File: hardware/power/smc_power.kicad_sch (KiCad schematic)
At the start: 64 parts, among them IC1 LM393DR2GH, J1 Screw_Terminal_Input, J2 Screw_Terminal_Output, Q1 P40B10SL, U1 TPS54360DDA, U2 AP2112K-3.3, U3 TPS54360DDA, U4 TL431D, U5 MCP1416, U7 L78L12_SOT89

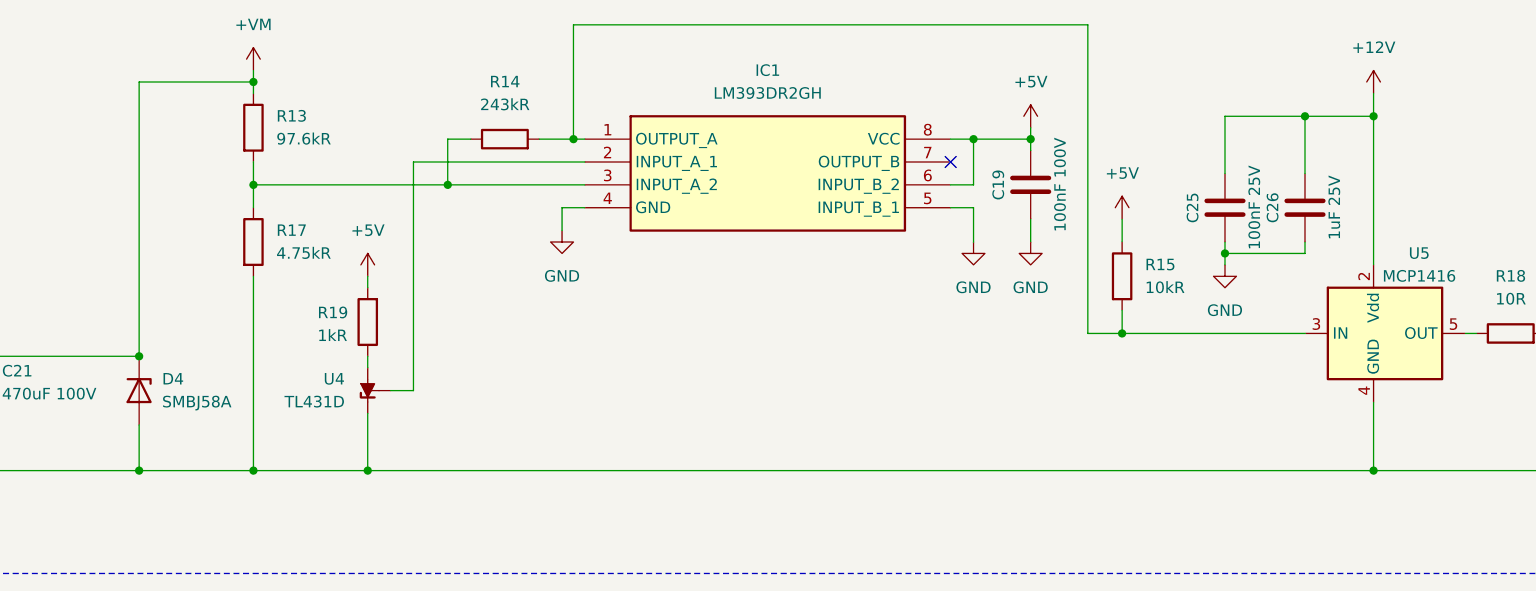
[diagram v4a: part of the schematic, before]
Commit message: hw(power): SMBJ51A TVS, fix TL431B (U4) orientation + REF-K, SOT-23 footprint, refs #35 #36 #37
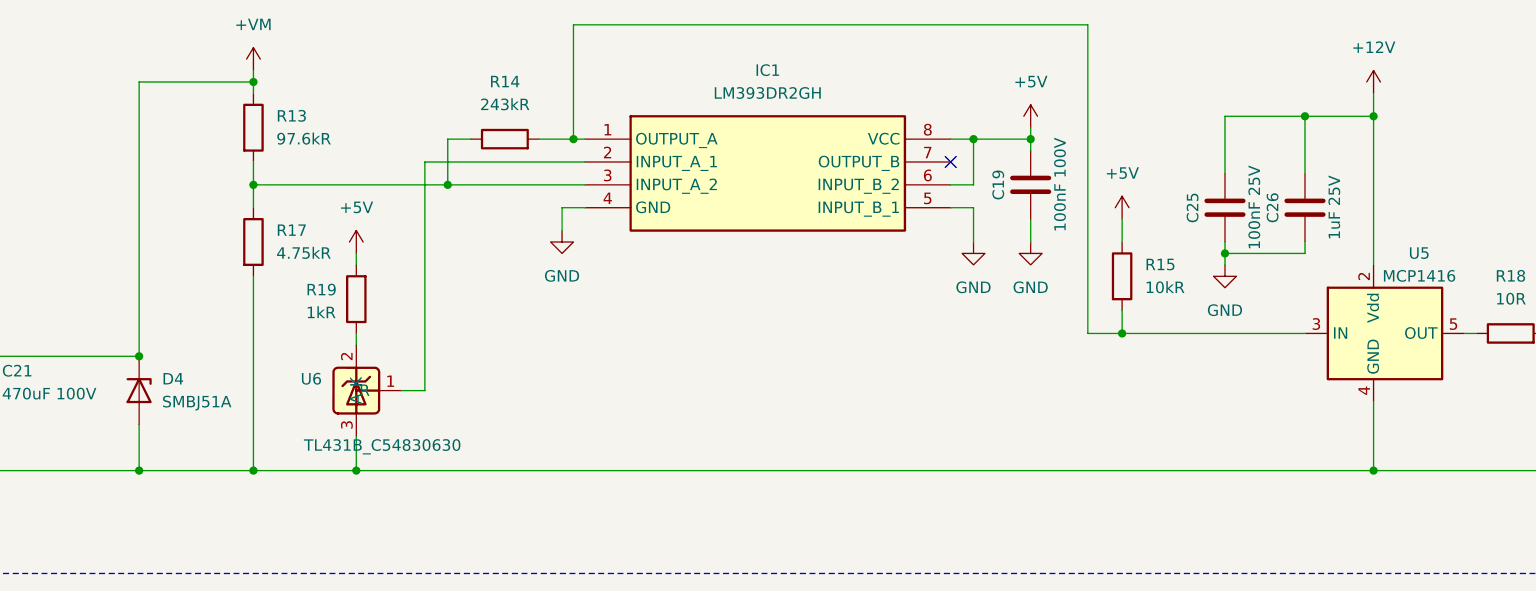
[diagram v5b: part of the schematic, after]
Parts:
- removed U4: TL431D, Package_SO:SOIC-8_3.9x4.9mm_P1.27mm, symbol Reference_Voltage:TL431D
- added U6: TL431B_C54830630, Package_TO_SOT_SMD:SOT-23-3, symbol JLCImport:TL431B_C54830630
- D4: value SMBJ58A -> SMBJ51A
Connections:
- net GND: now also U6.3 (A)
- net at R19.1: now also U6.2 (K)
- net at IC1.2 (INPUT_A_1): now also U6.1 (R)
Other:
- moved on the sheet: R19
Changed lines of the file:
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@@
 	)
 	(junction
-		(at 87.63 267.97)
-		(diameter 0)
-		(color 0 0 0 0)
-	)
-	(junction
 		(at 63.5 116.84)
 		(diameter 0)
@@
 	)
 	(junction
+		(at 86.36 267.97)
+		(diameter 0)
+		(color 0 0 0 0)
+	)
+	(junction
 		(at 62.23 167.64)
 		(diameter 0)
@@
 	(wire
 		(pts
+			(xy 86.36 264.16) (xy 86.36 267.97)
+		)
+		(stroke
+			(width 0)
+			(type default)
+		)
+	)
+	(wire
+		(pts
 			(xy 148.59 184.15) (xy 148.59 175.26)
 		)
@@
 	(wire
 		(pts
-			(xy 87.63 255.27) (xy 87.63 256.54)
+			(xy 86.36 252.73) (xy 86.36 254)
 		)
 		(stroke
@@
 	(wire
 		(pts
-			(xy 199.39 267.97) (xy 87.63 267.97)
+			(xy 74.93 267.97) (xy 86.36 267.97)
 		)
 		(stroke
@@
 	(wire
 		(pts
-			(xy 90.17 259.08) (xy 92.71 259.08)
-		)
-		(stroke
-			(width 0)
-			(type default)
-		)
-	)
-	(wire
-		(pts
 			(xy 114.3 121.92) (xy 114.3 137.16)
 		)
@@
 	(wire
 		(pts
-			(xy 87.63 246.38) (xy 87.63 247.65)
+			(xy 86.36 243.84) (xy 86.36 245.11)
 		)
 		(stroke
@@
 	(wire
 		(pts
-			(xy 92.71 233.68) (xy 111.76 233.68)
+			(xy 93.98 233.68) (xy 111.76 233.68)
 		)
 		(stroke
@@
 	(wire
 		(pts
+			(xy 86.36 267.97) (xy 199.39 267.97)
+		)
+		(stroke
+			(width 0)
+			(type default)
+		)
+	)
+	(wire
+		(pts
 			(xy 259.08 167.64) (xy 267.97 167.64)
 		)
@@
 	(wire
 		(pts
-			(xy 92.71 259.08) (xy 92.71 233.68)
+			(xy 93.98 259.08) (xy 93.98 233.68)
 		)
 		(stroke
@@
 	(wire
 		(pts
+			(xy 91.44 259.08) (xy 93.98 259.08)
+		)
+		(stroke
+			(width 0)
+			(type default)
+		)
+	)
+	(wire
+		(pts
 			(xy 181.61 185.42) (xy 181.61 187.96)
 		)
@@
 	(wire
 		(pts
-			(xy 74.93 267.97) (xy 87.63 267.97)
-		)
-		(stroke
-			(width 0)
-			(type default)
-		)
-	)
-	(wire
-		(pts
 			(xy 181.61 172.72) (xy 176.53 172.72)
 		)
@@
 	(wire
 		(pts
-			(xy 87.63 261.62) (xy 87.63 267.97)
-		)
-		(stroke
-			(width 0)
-			(type default)
-		)
-	)
-	(wire
-		(pts
 			(xy 134.62 198.12) (xy 134.62 200.66)
 		)
@@
 	(symbol
 		(lib_id "Device:R")
-		(at 87.63 251.46 180)
+		(at 86.36 248.92 180)
 		(unit 1)
 		(body_style 1)
@@
 		(dnp no)
 		(property "Reference" "R19"
-			(at 82.042 250.444 0)
+			(at 80.772 247.904 0)
 			(show_name no)
 			(do_not_autoplace no)
@@
 		)
 		(property "Value" "1kR"
-			(at 82.042 252.984 0)
+			(at 80.772 250.444 0)
 			(show_name no)
 			(do_not_autoplace no)
@@
 		)
 		(property "Footprint" "Resistor_SMD:R_0805_2012Metric_Pad1.20x1.40mm_HandSolder"
-			(at 89.408 251.46 90)
+			(at 88.138 248.92 90)
 			(hide yes)
 			(show_name no)
@@
 		)
 		(property "Datasheet" ""
-			(at 87.63 251.46 0)
+			(at 86.36 248.92 0)
 			(hide yes)
 			(show_name no)
@@
 		)
 		(property "Description" "Resistor"
-			(at 87.63 251.46 0)
+			(at 86.36 248.92 0)
 			(hide yes)
 			(show_name no)
@@
 	(symbol
 		(lib_id "power:+5V")
-		(at 87.63 246.38 0)
+		(at 86.36 243.84 0)
 		(unit 1)
 		(body_style 1)
@@
 		(fields_autoplaced yes)
 		(property "Reference" "#PWR025"
-			(at 87.63 250.19 0)
+			(at 86.36 247.65 0)
 			(hide yes)
 			(show_name no)
@@
 		)
 		(property "Value" "+5V"
-			(at 87.63 241.3 0)
+			(at 86.36 238.76 0)
 			(show_name no)
 			(do_not_autoplace no)
@@
 		)
 		(property "Footprint" ""
-			(at 87.63 246.38 0)
+			(at 86.36 243.84 0)
 			(hide yes)
 			(show_name no)
@@
 		)
 		(property "Datasheet" ""
-			(at 87.63 246.38 0)
+			(at 86.36 243.84 0)
 			(hide yes)
 			(show_name no)
@@
 		)
 		(property "Description" "Power symbol creates a global label with name \"+5V\""
-			(at 87.63 246.38 0)
+			(at 86.36 243.84 0)
 			(hide yes)
 			(show_name no)
@@
 	)
 	(symbol
-		(lib_id "Reference_Voltage:TL431D")
-		(at 87.63 259.08 270)
-		(unit 1)
-		(body_style 1)
-		(exclude_from_sim no)
-		(in_bom yes)
-		(on_board yes)
-		(in_pos_files yes)
-		(dnp no)
-		(fields_autoplaced yes)
-		(property "Reference" "U4"
-			(at 85.09 257.8099 90)
-			(show_name no)
-			(do_not_autoplace no)
-			(effects
-				(font
-					(size 1.27 1.27)
-				)
-				(justify right)
-			)
-		)
-		(property "Value" "TL431D"
-			(at 85.09 260.3499 90)
-			(show_name no)
-			(do_not_autoplace no)
-			(effects
-				(font
-					(size 1.27 1.27)
-				)
-				(justify right)
-			)
-		)
-		(property "Footprint" "Package_SO:SOIC-8_3.9x4.9mm_P1.27mm"
-			(at 81.28 259.08 0)
-			(hide yes)
-			(show_name no)
-			(do_not_autoplace no)
-			(effects
-				(font
-					(size 1.27 1.27)
-					(italic yes)
-				)
-			)
-		)
-		(property "Datasheet" "http://www.ti.com/lit/ds/symlink/tl431.pdf"
-			(at 76.962 259.334 0)
-			(hide yes)
-			(show_name no)
-			(do_not_autoplace no)
-			(effects
-				(font
-					(size 1.27 1.27)
-					(italic yes)
-				)
-			)
-		)
-		(property "Description" "Shunt Regulator, SO-8"
-			(at 79.248 258.826 0)
-			(hide yes)
-			(show_name no)
-			(do_not_autoplace no)
-			(effects
-				(font
-					(size 1.27 1.27)
-				)
-			)
-		)
-		(pin "1"
-		)
-		(pin "8"
-		)
-		(pin "[2,3,6,7]"
-		)
-		(instances
-			(project "smc_power"
-				(path "/30583e29-7231-44d2-b6ef-f52f82bb6e27"
-					(reference "U4")
-					(unit 1)
-				)
-			)
-		)
-	)
-	(symbol
 		(lib_id "Regulator_Linear:AP2112K-3.3")
 		(at 284.48 114.3 0)
@@
 	)
 	(symbol
+		(lib_id "JLCImport:TL431B_C54830630")
+		(at 86.36 259.08 0)
+		(mirror y)
+		(unit 1)
+		(body_style 1)
+		(exclude_from_sim no)
+		(in_bom yes)
+		(on_board yes)
+		(in_pos_files yes)
+		(dnp no)
+		(property "Reference" "U6"
+			(at 82.55 257.8099 0)
+			(show_name no)
+			(do_not_autoplace no)
+			(effects
+				(font
+					(size 1.27 1.27)
+				)
+				(justify left)
+			)
+		)
+		(property "Value" "TL431B_C54830630"
+			(at 98.044 265.176 0)
+			(show_name no)
+			(do_not_autoplace no)
+			(effects
+				(font
+					(size 1.27 1.27)
+				)
+				(justify left)
+			)
+		)
+		(property "Footprint" "Package_TO_SOT_SMD:SOT-23-3"
+			(at 86.36 259.08 0)
+			(hide yes)
+			(show_name no)
+			(do_not_autoplace no)
+			(effects
+				(font
+					(size 1.27 1.27)
+				)
+			)
+		)
+		(property "Datasheet" "https://item.szlcsc.com/139341.html"
+			(at 86.36 259.08 0)
+			(hide yes)
+			(show_name no)
+			(do_not_autoplace no)
+			(effects
+				(font
+					(size 1.27 1.27)
+				)
+			)
+		)
+		(property "Description" "-20℃~+70℃@(Ta) 150mA 1uA 2.5V~36V 2.5V~36V 250uA Adjustable Parallel ±0.3% SOT-23 Voltage Reference ROHS"
+			(at 86.36 259.08 0)
+			(hide yes)
+			(show_name no)
+			(do_not_autoplace no)
+			(effects
+				(font
+					(size 1.27 1.27)
+				)
+			)
+		)
+		(property "LCSC" "C54830630"
+			(at 86.36 259.08 0)
+			(hide yes)
+			(show_name no)
+			(do_not_autoplace no)
+			(effects
+				(font
+					(size 1.27 1.27)
+				)
+			)
+		)
+		(property "Manufacturer" "hongjiacheng"
+			(at 86.36 259.08 0)
+			(hide yes)
+			(show_name no)
+			(do_not_autoplace no)
+			(effects
+				(font
+					(size 1.27 1.27)
+				)
+			)
+		)
+		(property "Manufacturer Part" "TL431B"
+			(at 86.36 259.08 0)
+			(hide yes)
+			(show_name no)
+			(do_not_autoplace no)
+			(effects
+				(font
+					(size 1.27 1.27)
+				)
+			)
+		)
+		(pin "3"
+		)
+		(pin "1"
+		)
+		(pin "2"
+		)
+		(instances
+			(project "smc_power"
+				(path "/30583e29-7231-44d2-b6ef-f52f82bb6e27"
+					(reference "U6")
+					(unit 1)
+				)
+			)
+		)
+	)
+	(symbol
 		(lib_id "Device:R")
 		(at 135.89 118.11 0)
@@
 			)
 		)
-		(property "Value" "SMBJ58A"
+		(property "Value" "SMBJ51A"
 			(at 64.77 260.3499 90)
 			(show_name no)

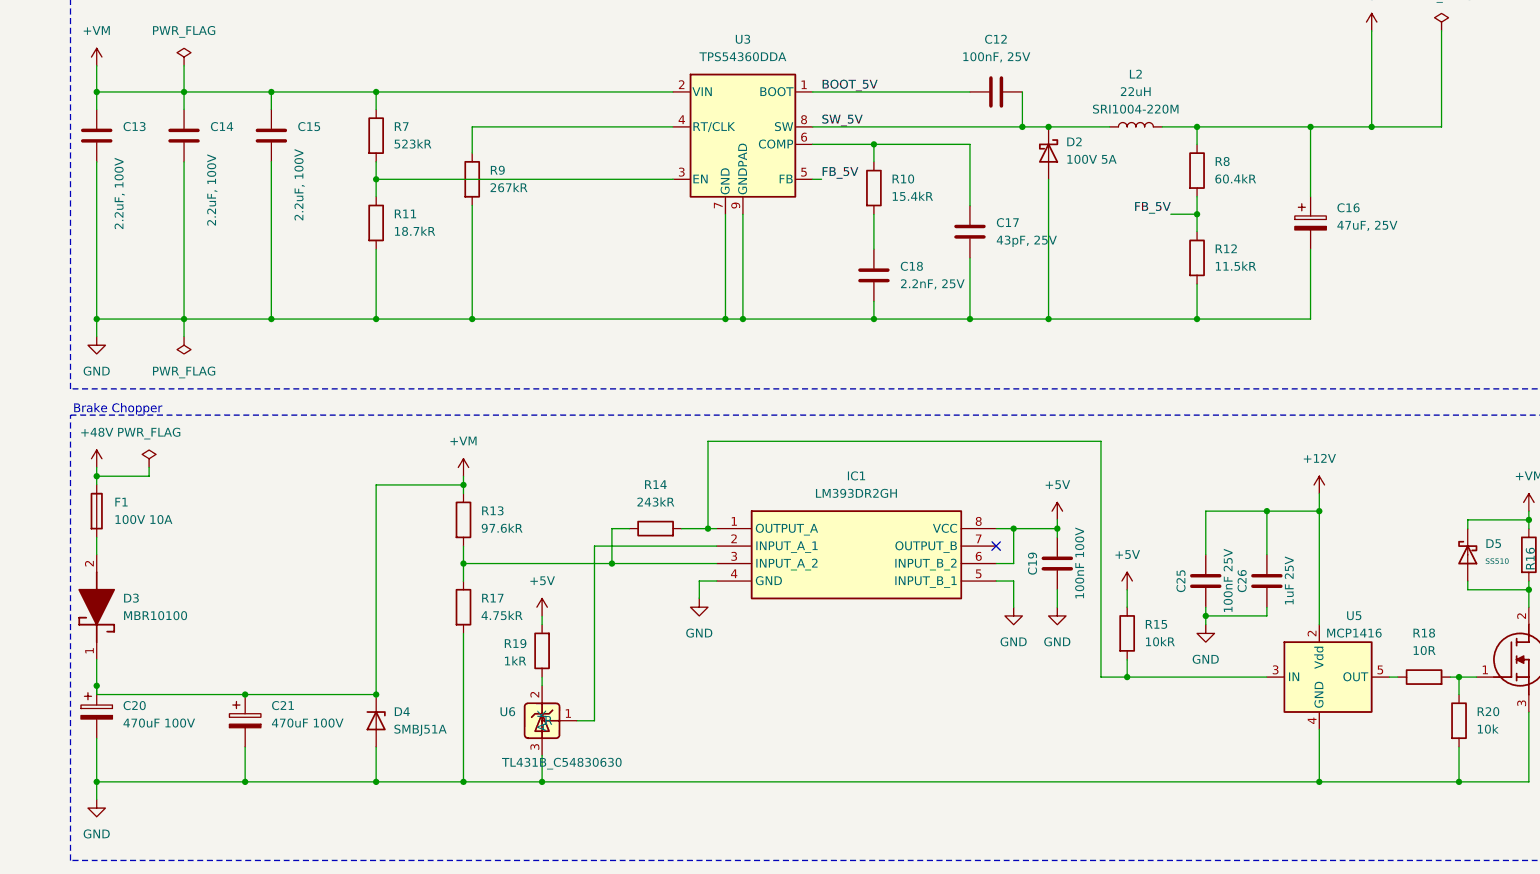
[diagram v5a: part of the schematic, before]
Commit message: hw(power): 5V output 2x22uF X7R + recompensation, inrush NTC, C22-24 footprints, refs #35, closes #38
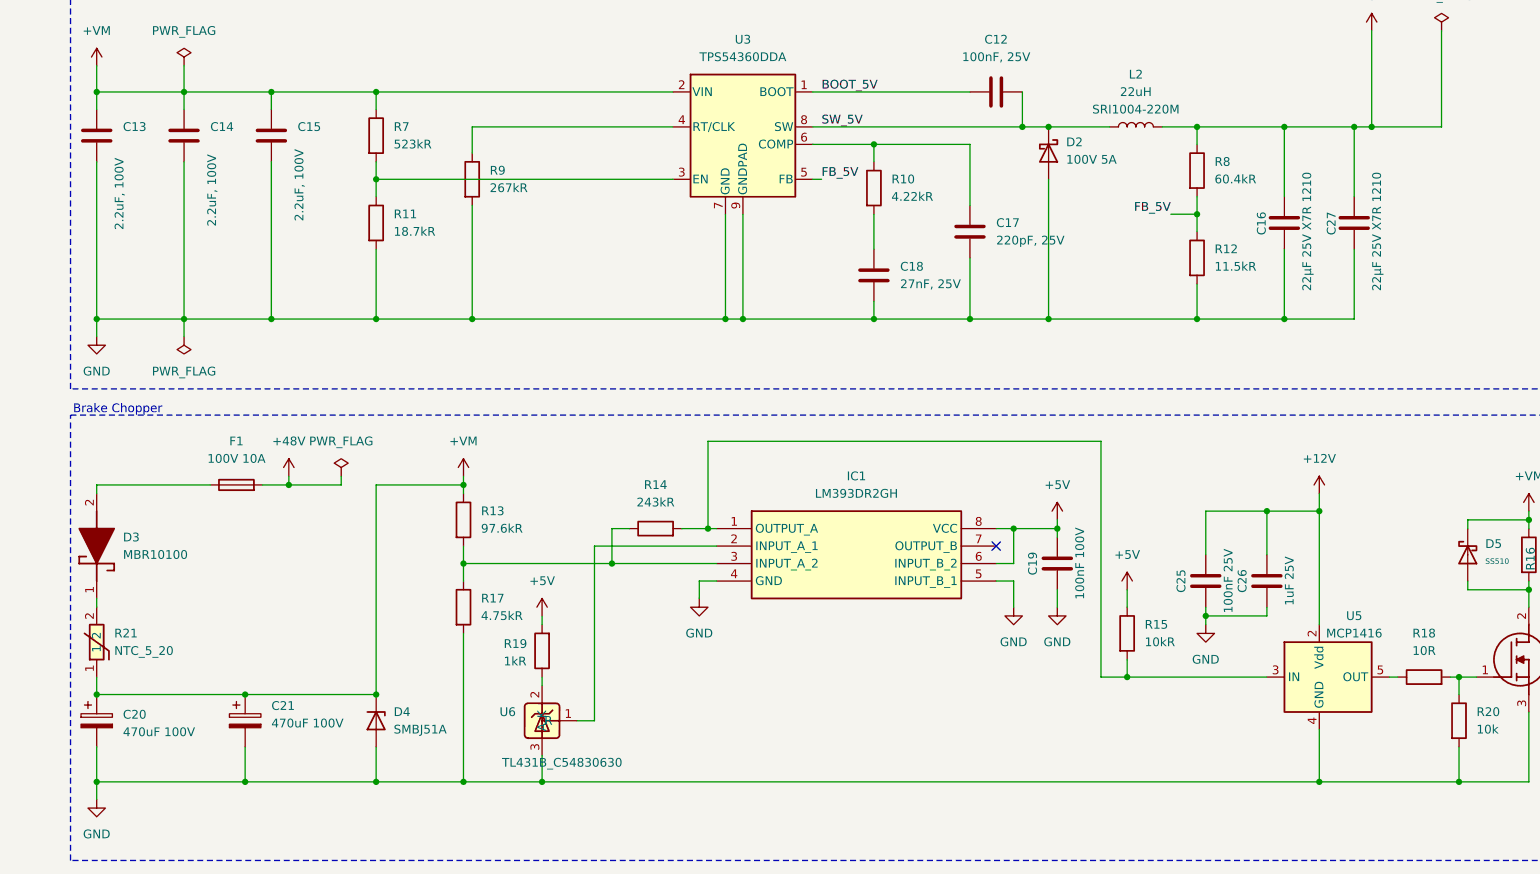
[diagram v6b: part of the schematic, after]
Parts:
- removed C16: 47uF, 25V, Capacitor_THT:CP_Radial_D5.0mm_P2.50mm, symbol Device:C_Polarized
- added C16, C27: 22µF 25V X7R 1210, symbol Device:C
- added R21: NTC_5_20, Connector_Phoenix_SPT:PhoenixContact_SPT_5_1-V-7.5_1x01_P7.5mm_Vertical, symbol JLCImport:NTC_5_20
- C17: value 43pF, 25V -> 220pF, 25V
- C18: value 2.2nF, 25V -> 27nF, 25V
- R10: value 15.4kR -> 4.22kR
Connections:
- net +48V: now also F1.2; no longer F1.1
- net +5V: now also C16.1, C27.1
- net +VM: now also R21.1; no longer D3.1 (K)
- net GND: now also C16.2, C27.2
- net at D3.2 (A): now also F1.1; no longer F1.2
- new net: D3.1 (K), R21.2
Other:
- moved on the sheet: C20, D3, F1
